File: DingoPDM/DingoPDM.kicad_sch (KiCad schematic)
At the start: 6 parts

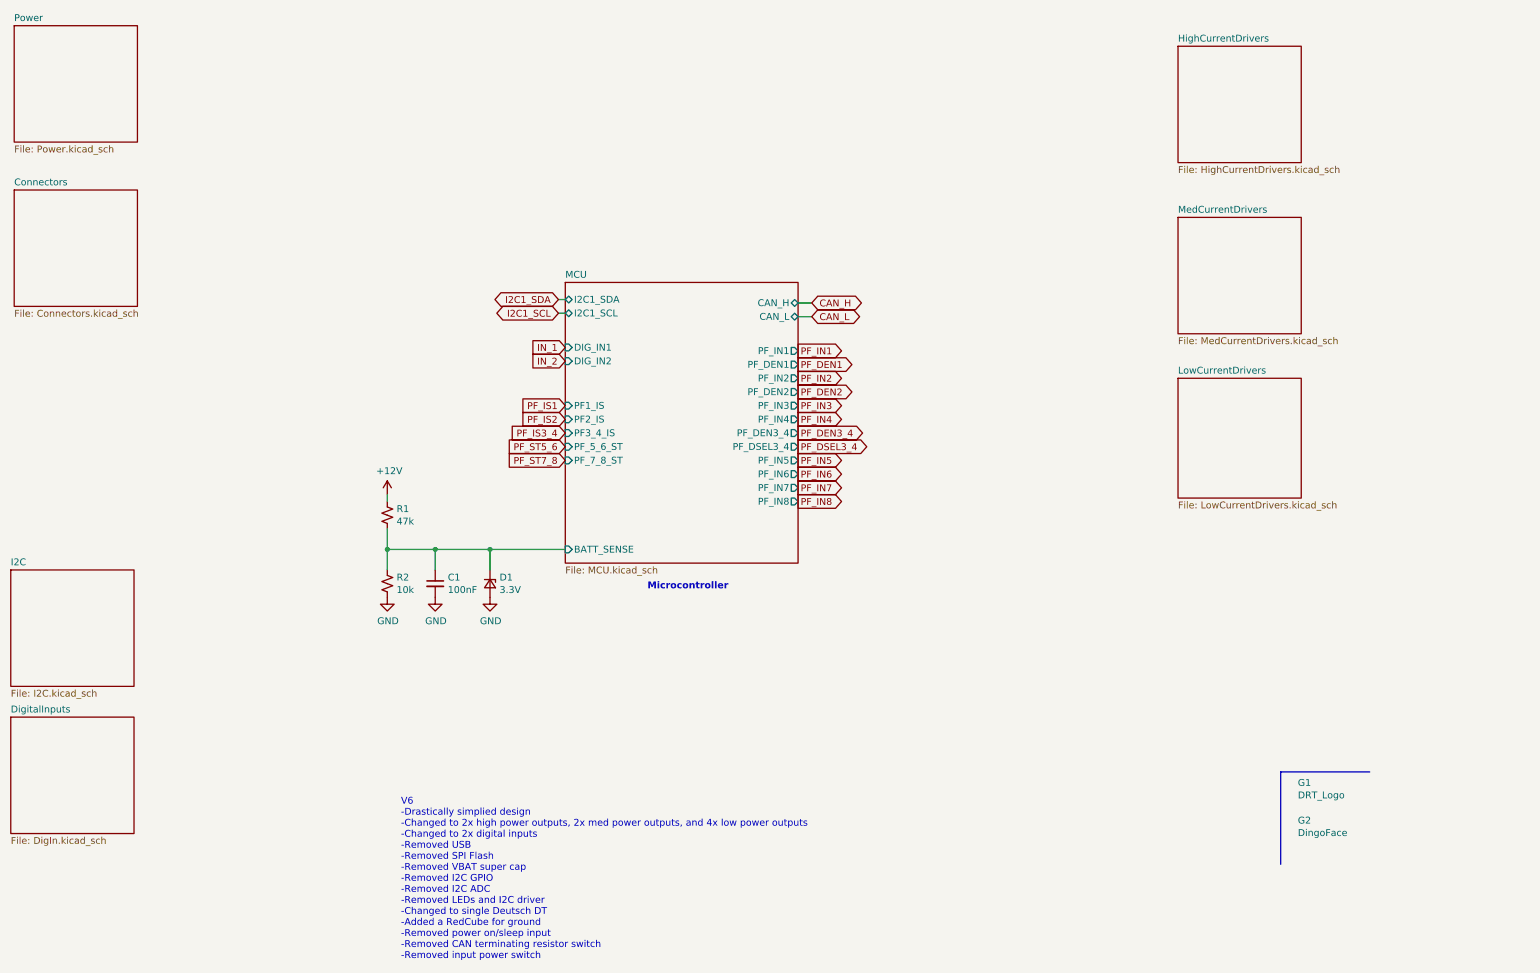
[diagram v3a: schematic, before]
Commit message: Changed to STM32F446RE
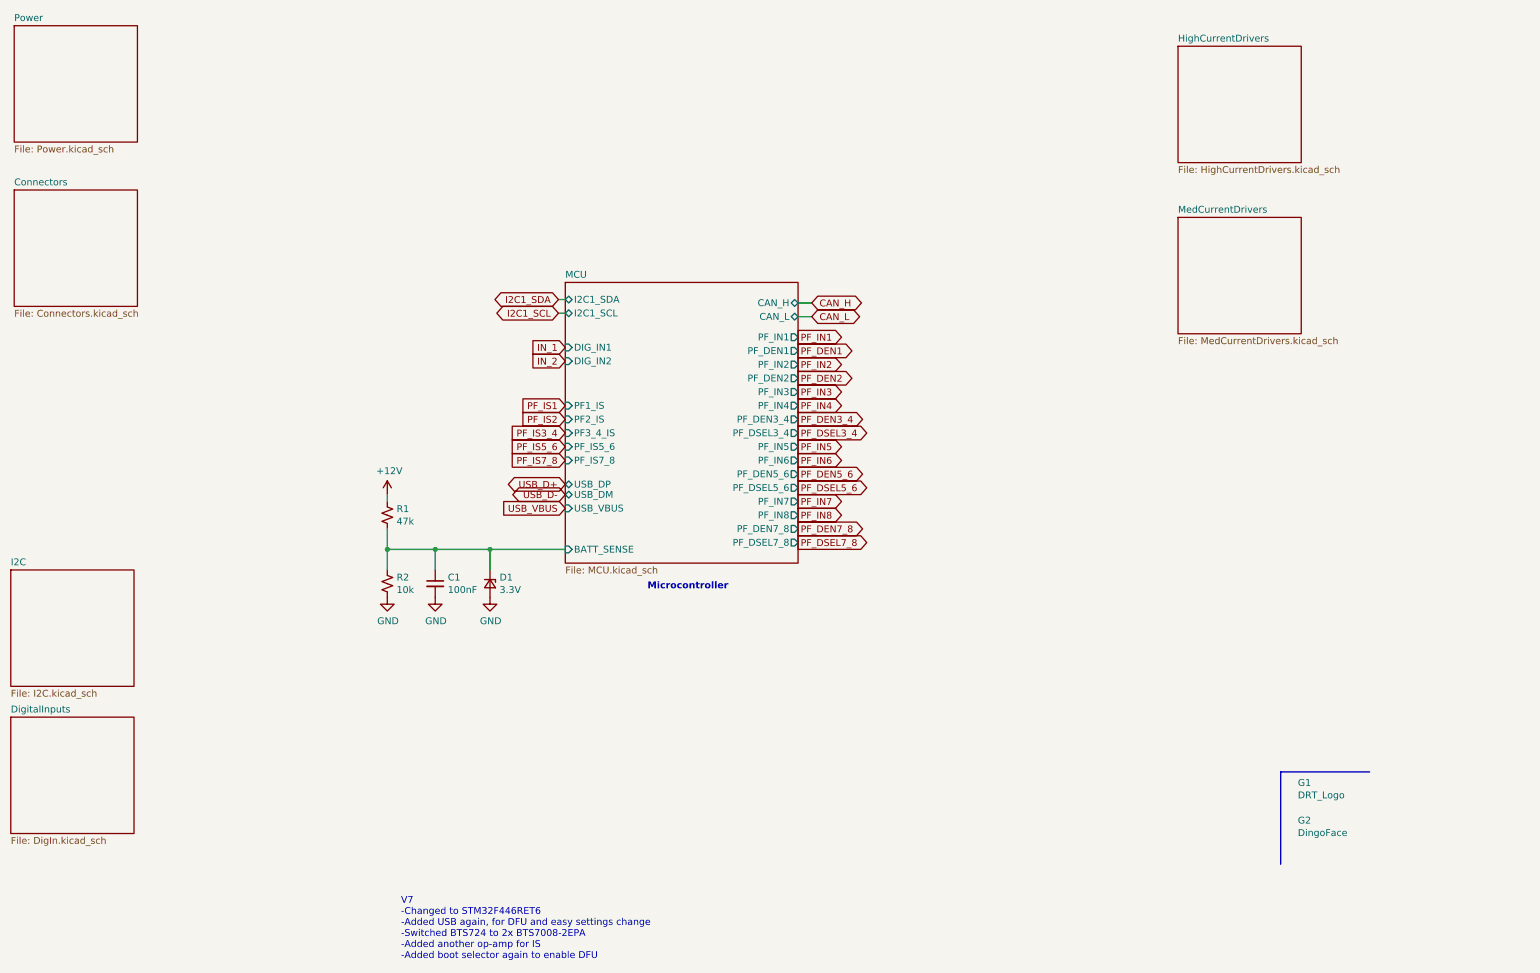
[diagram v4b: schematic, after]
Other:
- removed sheet LowCurrentDrivers
- sheet MCU ports: added PF_DEN5_6, PF_DEN7_8, PF_DSEL5_6, PF_DSEL7_8, PF_IS5_6, PF_IS7_8, USB_DM, USB_DP, USB_VBUS; removed PF_5_6_ST, PF_7_8_ST
- note added: "V7 -Changed to STM32F446RET6 -Added USB again, for DFU and easy settings change -Switched BTS724 to 2x BTS7008-2EPA -Added another op-amp for IS -Added boot selector again to enable DFU"
- note removed: "V6 -Drastically simplied design -Changed to 2x high power outputs, 2x med power outputs, and 4x low power outputs -Changed to 2x digital inputs -Removed USB -Removed SPI Flash -Removed VBAT super cap -Removed I2C GPIO -Removed I2C ADC -Removed LEDs and I2C driver -Changed to single Deutsch DT -Added a RedCube for ground -Removed power on/sleep input -Removed CAN terminating resistor switch -Remov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"

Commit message: Small edits
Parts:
- R1: value 47k -> 47K
- R2: value 10k -> 10K
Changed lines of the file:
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@@
       (effects (font (size 1.27 1.27)) (justify left))
     )
-    (property "Value" "47k" (at 86.1822 107.823 0)
+    (property "Value" "47K" (at 86.1822 107.823 0)
       (effects (font (size 1.27 1.27)) (justify left))
     )
@@
       (effects (font (size 1.27 1.27)) (justify left))
     )
-    (property "Value" "10k" (at 86.1822 120.523 0)
+    (property "Value" "10K" (at 86.1822 120.523 0)
       (effects (font (size 1.27 1.27)) (justify left))
     )

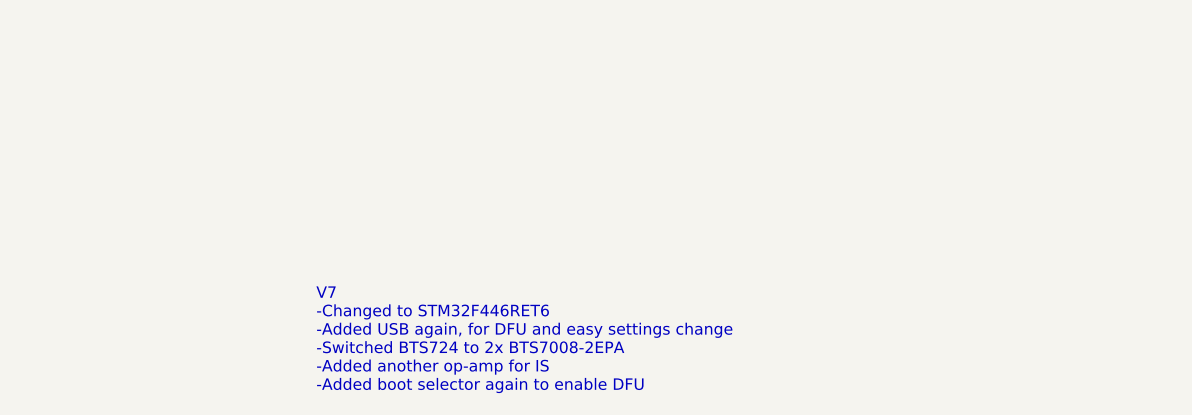
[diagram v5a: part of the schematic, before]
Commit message: V7.1 Fixes
SDA/SCL mixed up on FRAM, added status LEDs, switched to thermal relief zones
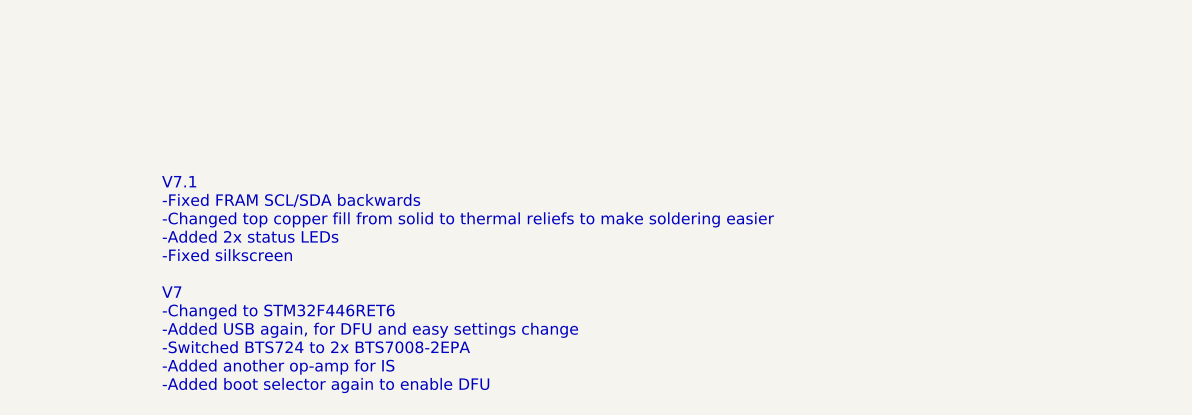
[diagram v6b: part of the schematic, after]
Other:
- note added: "V7.1 -Fixed FRAM SCL/SDA backwards -Changed top copper fill from solid to thermal reliefs to make soldering easier -Added 2x status LEDs -Fixed silkscreen V7 -Changed to STM32F446RET6 -Added USB again, for DFU and easy settings change -Switched BTS724 to 2x BTS7008-2EPA -Added another op-amp for IS -Added boot selector again to enable DFU"
- note removed: "V7 -Changed to STM32F446RET6 -Added USB again, for DFU and easy settings change -Switched BTS724 to 2x BTS7008-2EPA -Added another op-amp for IS -Added boot selector again to enable DFU"
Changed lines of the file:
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@@
   (title_block
     (title "Dingo_PDM")
-    (date "2023-07-28")
-    (rev "v6")
+    (date "2023-09-04")
+    (rev "v7.1")
     (comment 3 "github.com/corygrant")
     (comment 4 "Cory Grant")
@@
     (effects (font (size 1.27 1.27) (thickness 0.254) bold) (justify left bottom))
   )
-  (text "V7\n-Changed to STM32F446RET6\n-Added USB again, for DFU and easy settings change\n-Switched BTS724 to 2x BTS7008-2EPA\n-Added another op-amp for IS\n-Added boot selector again to enable DFU\n"
-    (at 86.995 189.23 0)
+  (text "V7.1\n-Fixed FRAM SCL/SDA backwards\n-Changed top copper fill from solid to thermal reliefs to make soldering easier\n-Added 2x status LEDs\n-Fixed silkscreen\n\nV7\n-Changed to STM32F446RET6\n-Added USB again, for DFU and easy settings change\n-Switched BTS724 to 2x BTS7008-2EPA\n-Added another op-amp for IS\n-Added boot selector again to enable DFU\n"
+    (at 69.85 189.23 0)
     (effects (font (size 1.27 1.27)) (justify left bottom))
   )

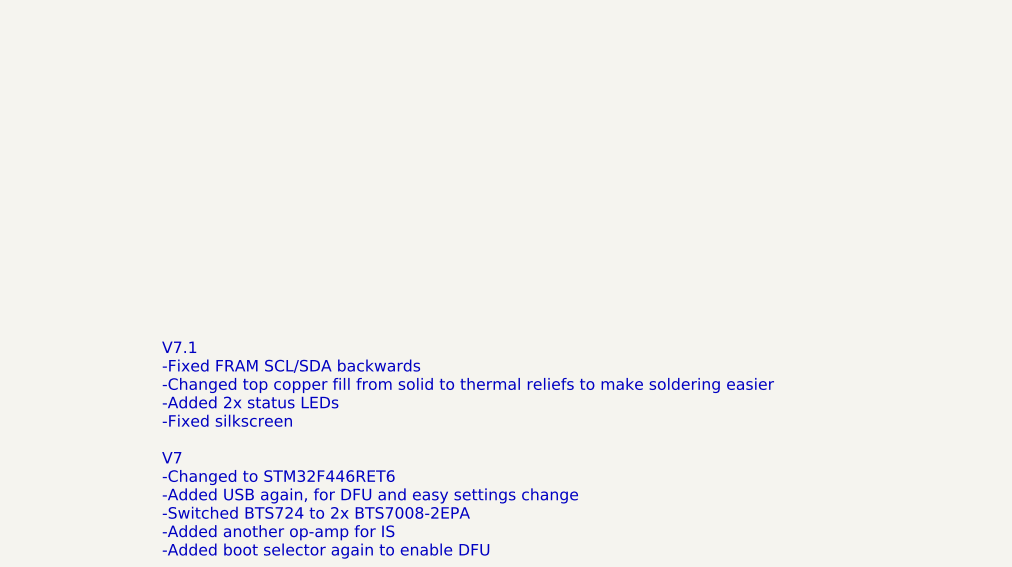
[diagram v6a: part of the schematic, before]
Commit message: Add diode, disconnect PB13, fix USB VBUS
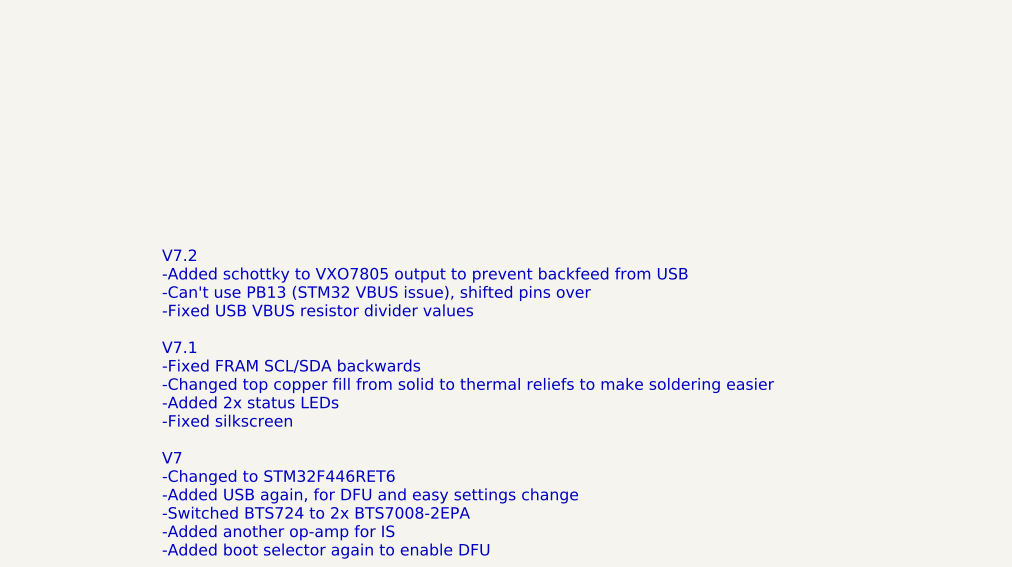
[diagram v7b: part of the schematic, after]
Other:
- note added: "V7.2 -Added schottky to VXO7805 output to prevent backfeed from USB -Can't use PB13 (STM32 VBUS issue), shifted pins over -Fixed USB VBUS resistor divider values V7.1 -Fixed FRAM SCL/SDA backwards -Changed top copper fill from solid to thermal reliefs to make soldering easier -Added 2x status LEDs -Fixed silkscreen V7 -Changed to STM32F446RET6 -Added USB again, for DFU and easy settings change -S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"
- note removed: "V7.1 -Fixed FRAM SCL/SDA backwards -Changed top copper fill from solid to thermal reliefs to make soldering easier -Added 2x status LEDs -Fixed silkscreen V7 -Changed to STM32F446RET6 -Added USB again, for DFU and easy settings change -Switched BTS724 to 2x BTS7008-2EPA -Added another op-amp for IS -Added boot selector again to enable DFU"
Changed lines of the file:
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@@
   (title_block
     (title "Dingo_PDM")
-    (date "2023-09-04")
-    (rev "v7.1")
+    (date "2023-09-11")
+    (rev "v7.2")
     (comment 3 "github.com/corygrant")
     (comment 4 "Cory Grant")
@@
     (effects (font (size 1.27 1.27) (thickness 0.254) bold) (justify left bottom))
   )
-  (text "V7.1\n-Fixed FRAM SCL/SDA backwards\n-Changed top copper fill from solid to thermal reliefs to make soldering easier\n-Added 2x status LEDs\n-Fixed silkscreen\n\nV7\n-Changed to STM32F446RET6\n-Added USB again, for DFU and easy settings change\n-Switched BTS724 to 2x BTS7008-2EPA\n-Added another op-amp for IS\n-Added boot selector again to enable DFU\n"
+  (text "V7.2\n-Added schottky to VXO7805 output to prevent backfeed from USB\n-Can't use PB13 (STM32 VBUS issue), shifted pins over\n-Fixed USB VBUS resistor divider values\n\nV7.1\n-Fixed FRAM SCL/SDA backwards\n-Changed top copper fill from solid to thermal reliefs to make soldering easier\n-Added 2x status LEDs\n-Fixed silkscreen\n\nV7\n-Changed to STM32F446RET6\n-Added USB again, for DFU and easy settings change\n-Switched BTS724 to 2x BTS7008-2EPA\n-Added another op-amp for IS\n-Added boot selector again to enable DFU\n"
     (at 69.85 189.23 0)
     (effects (font (size 1.27 1.27)) (justify left bottom))

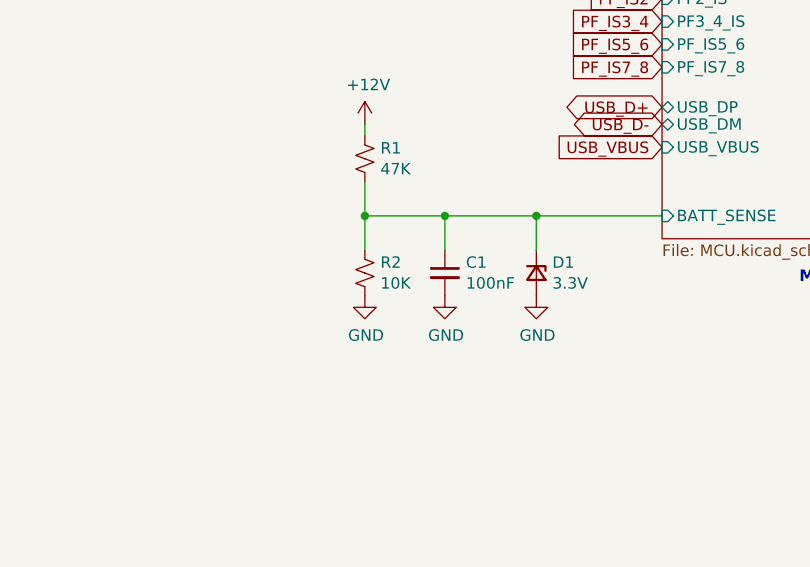
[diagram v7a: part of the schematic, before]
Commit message: Updated JLC zener diode part and batt volt divider
The previous zener diode had too low of a breakdown zener voltage.
The previous voltage divider was also too high of an output voltage, swapped R2 to lower the max voltage to well below the breakdown zener voltage
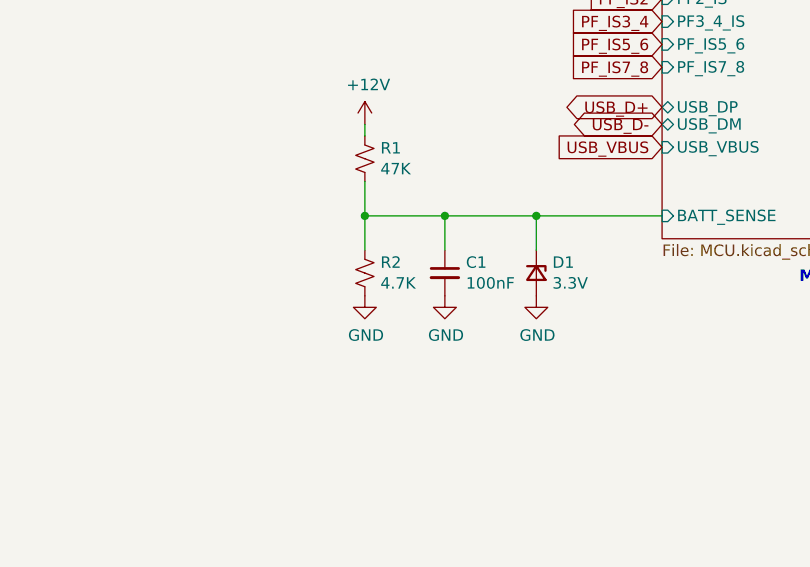
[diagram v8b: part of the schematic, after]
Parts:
- D1: LCSC C177016 -> C426855
- R2: value 10K -> 4.7K; Digi-Key_PN 311-10.0KCRDKR-ND -> 311-4.70KCRCT-ND; LCSC C17414 -> C17673
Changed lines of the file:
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@@
       (effects (font (size 1.27 1.27)) (justify left))
     )
-    (property "Value" "10K" (at 86.1822 120.523 0)
+    (property "Value" "4.7K" (at 86.1822 120.523 0)
       (effects (font (size 1.27 1.27)) (justify left))
     )
@@
       (effects (font (size 1.27 1.27)) hide)
     )
-    (property "Digi-Key_PN" "311-10.0KCRDKR-ND" (at 84.455 119.38 0)
+    (property "Digi-Key_PN" "311-4.70KCRCT-ND" (at 84.455 119.38 0)
       (effects (font (size 1.27 1.27)) hide)
     )
-    (property "LCSC" "C17414" (at 84.455 119.38 0)
+    (property "LCSC" "C17673" (at 84.455 119.38 0)
       (effects (font (size 1.27 1.27)) hide)
     )
@@
       (effects (font (size 1.27 1.27)) hide)
     )
-    (property "LCSC" "C177016" (at 103.505 119.38 0)
+    (property "LCSC" "C426855" (at 103.505 119.38 0)
       (effects (font (size 1.27 1.27)) hide)
     )
